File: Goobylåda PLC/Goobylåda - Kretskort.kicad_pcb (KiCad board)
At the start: 2 copper layers, 100 x 100 mm, 99 parts, among them J1 LCD 1602 kontakt, J10 Anslutning, J11 Anslutning, J12 Anslutning, J13 Anslutning, J14 Anslutning, J15 Anslutning, J16 Anslutning, J17 Anslutning, J18 Anslutning, J2 Anslutning, J3 Anslutning, J4 Anslutning, J5 Anslutning, J6 Anslutning, J7 Anslutning, J8 Anslutning, J9 Anslutning, Q1 2N2222, Q10 MJE2955T, Q11 MJE2955T, Q12 MJE2955T, Q2 2N2222, Q3 2N2222, Q4 IRF9630, Q5 IRF9630, Q6 IRF9630, Q7 2N2222, Q8 2N2222, Q9 2N2222, U1 LM7812_TO220

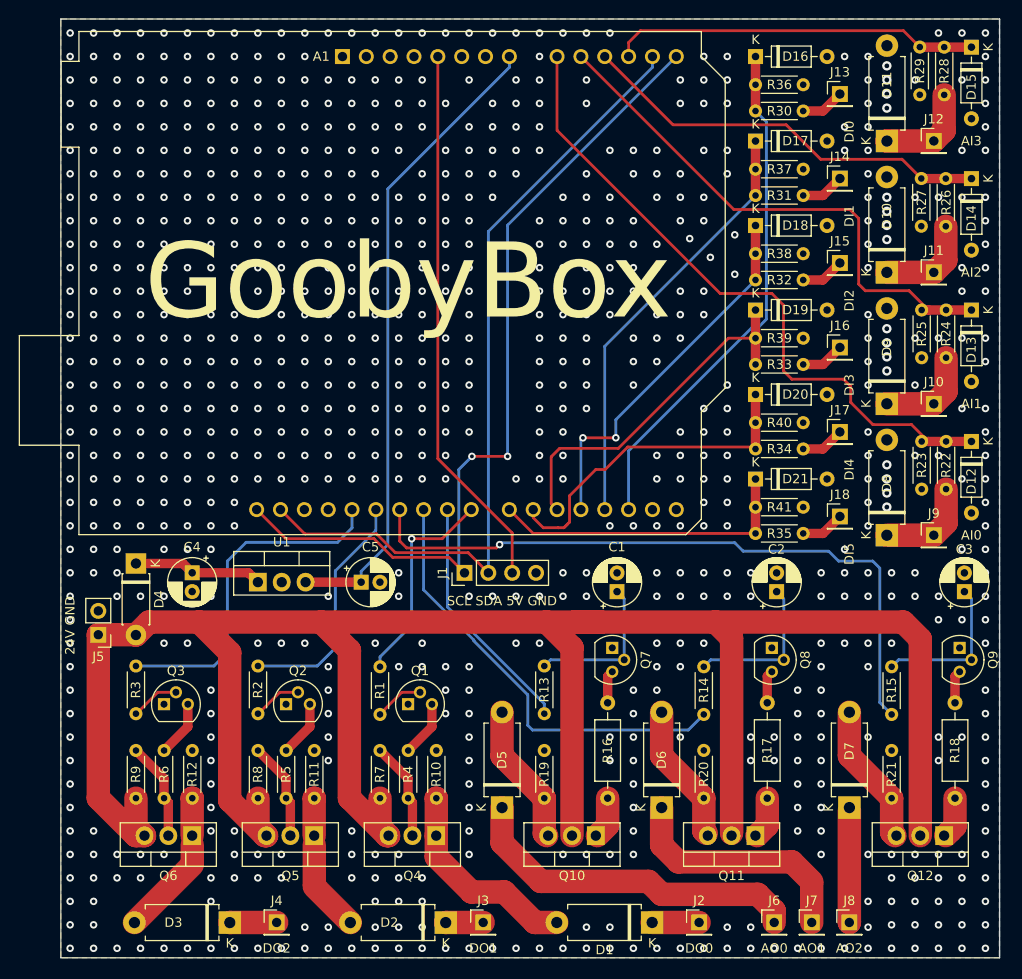
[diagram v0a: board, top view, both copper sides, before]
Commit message: Update for THT
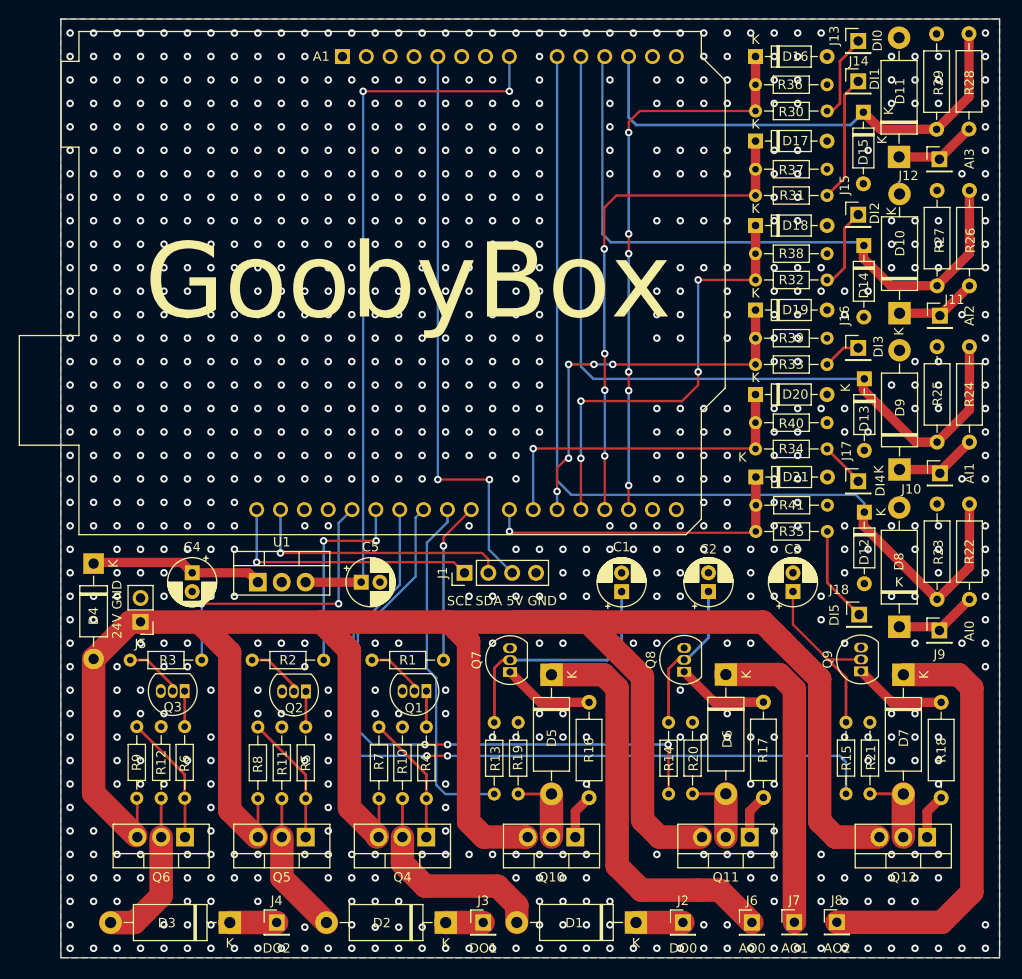
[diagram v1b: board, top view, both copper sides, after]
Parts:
- D1, D10, D11, D2, D3, D5, D6, D7, D8, D9: footprint Diode_THT:D_DO-15_P10.16mm_Horizontal -> Diode_THT:D_DO-15_P12.70mm_Horizontal
- D4: footprint Diode_THT:D_DO-41_SOD81_P7.62mm_Horizontal -> Diode_THT:D_DO-41_SOD81_P10.16mm_Horizontal
- Q1, Q2, Q3, Q7, Q8, Q9: value 2N2222 -> 2N2222; footprint Package_TO_SOT_THT:TO-92 -> Package_TO_SOT_THT:TO-92_Inline
- Q10, Q11, Q12: value MJE2955T -> MJE29555T
- R1, R10, R11, R12, R13, R14, R15, R19, R2, R20, R21, R3, R30, R31, R32, R33, R34, R35, R36, R37, R38, R39, R4, R40, R41, R5, R6, R7, R8, R9: footprint Resistor_THT:R_Axial_DIN0204_L3.6mm_D1.6mm_P5.08mm_Horizontal -> Resistor_THT:R_Axial_DIN0204_L3.6mm_D1.6mm_P7.62mm_Horizontal
- R22, R23, R24, R25, R26, R27, R28, R29: footprint Resistor_THT:R_Axial_DIN0204_L3.6mm_D1.6mm_P5.08mm_Horizontal -> Resistor_THT:R_Axial_DIN0207_L6.3mm_D2.5mm_P10.16mm_Horizontal
- moved C3 18.3 mm to (167.0, 102.0)
- moved R23 16.9 mm to (182.3, 102.8), turned to 90 degrees
- moved D6 15.7 mm to (159.8, 110.8), turned to -90 degrees
- moved D7 15.3 mm to (178.8, 110.9), turned to -90 degrees
- moved D5 15.1 mm to (141.3, 110.9), turned to -90 degrees
- moved R25 14.2 mm to (182.3, 86.1), turned to 90 degrees
- moved D12 13.7 mm to (174.6, 93.5)
- moved D13 13.6 mm to (174.6, 79.3)
- moved D14 13.5 mm to (174.6, 65.1)
- moved D15 13.4 mm to (174.5, 50.9)
- moved R22 12.0 mm to (185.8, 102.8)
- moved R27 11.6 mm to (182.3, 69.4), turned to 90 degrees
- moved Q7 11.2 mm to (136.9, 110.6), turned to 90 degrees
- moved Q9 10.8 mm to (174.2, 110.5), turned to 90 degrees
- moved J18 10.6 mm to (174.1, 104.5)
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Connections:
- A1 pad 13: /SDA -> unconnected-(A1-Pad13)
- A1 pad 14: /SCL -> unconnected-(A1-Pad14)
- Q1 pad 1: GND -> Net-(Q1-Pad1)
- Q1 pad 3: Net-(Q1-Pad3) -> GND
- Q10 pad 2: +24V -> Net-(D5-Pad2)
- Q10 pad 3: Net-(D5-Pad2) -> +24V
- Q11 pad 2: +24V -> Net-(D6-Pad2)
- Q11 pad 3: Net-(D6-Pad2) -> +24V
- Q12 pad 2: +24V -> Net-(D7-Pad2)
- Q12 pad 3: Net-(D7-Pad2) -> +24V
- Q2 pad 1: GND -> Net-(Q2-Pad1)
- Q2 pad 3: Net-(Q2-Pad3) -> GND
- Q3 pad 1: GND -> Net-(Q3-Pad1)
- Q3 pad 3: Net-(Q3-Pad3) -> GND
- Q4 pad 1: Net-(D1-Pad2) -> Net-(Q4-Pad1)
- Q4 pad 2: Net-(Q4-Pad2) -> Net-(D1-Pad2)
- Q5 pad 1: Net-(D2-Pad2) -> Net-(Q5-Pad1)
- Q5 pad 2: Net-(Q5-Pad2) -> Net-(D2-Pad2)
- Q6 pad 1: Net-(D3-Pad2) -> Net-(Q6-Pad1)
- Q6 pad 2: Net-(Q6-Pad2) -> Net-(D3-Pad2)
- Q7 pad 1: GND -> Net-(Q7-Pad1)
- Q7 pad 3: Net-(Q7-Pad3) -> GND
- Q8 pad 1: GND -> Net-(Q8-Pad1)
- Q8 pad 3: Net-(Q8-Pad3) -> GND
- Q9 pad 1: GND -> Net-(Q9-Pad1)
- Q9 pad 3: Net-(Q9-Pad3) -> GND
- R16 pad 2: Net-(Q7-Pad3) -> Net-(Q7-Pad1)
- R17 pad 2: Net-(Q8-Pad3) -> Net-(Q8-Pad1)
- R18 pad 2: Net-(Q9-Pad3) -> Net-(Q9-Pad1)
- R4 pad 1: Net-(Q4-Pad2) -> Net-(Q4-Pad1)
- R4 pad 2: Net-(Q1-Pad3) -> Net-(Q1-Pad1)
- R5 pad 1: Net-(Q5-Pad2) -> Net-(Q5-Pad1)
- R5 pad 2: Net-(Q2-Pad3) -> Net-(Q2-Pad1)
- R6 pad 1: Net-(Q6-Pad2) -> Net-(Q6-Pad1)
- R6 pad 2: Net-(Q3-Pad3) -> Net-(Q3-Pad1)
- R7 pad 2: Net-(Q4-Pad2) -> Net-(Q4-Pad1)
- R8 pad 2: Net-(Q5-Pad2) -> Net-(Q5-Pad1)
- R9 pad 2: Net-(Q6-Pad2) -> Net-(Q6-Pad1)
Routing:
- net /SCL: track 92.0 -> 28.2 mm, vias 2 -> 1
- net /SDA: track 87.2 -> 28.5 mm, vias 0 -> 1
- net /AO_2: track 12.0 -> 45.3 mm
- net /A0: track 71.5 -> 104.0 mm
- net /A1: track 57.6 -> 86.7 mm
- net /A2: track 44.4 -> 69.4 mm
- net /D10: track 47.2 -> 65.4 mm, vias 0 -> 3
- net Net-(Q6-Pad1): track 0.00 -> 13.9 mm
- net Net-(Q4-Pad1): track 0.00 -> 13.8 mm
- net Net-(Q5-Pad1): track 0.00 -> 13.7 mm
- net /A3: track 39.3 -> 52.6 mm
- net /D11: track 72.3 -> 84.7 mm, vias 1 -> 2
- net /D9: track 26.0 -> 37.2 mm
- net Net-(Q4-Pad2): track 10.5 -> 0.00 mm
- net Net-(Q6-Pad2): track 10.5 -> 0.00 mm
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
